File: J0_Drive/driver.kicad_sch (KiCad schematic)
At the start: 7 parts

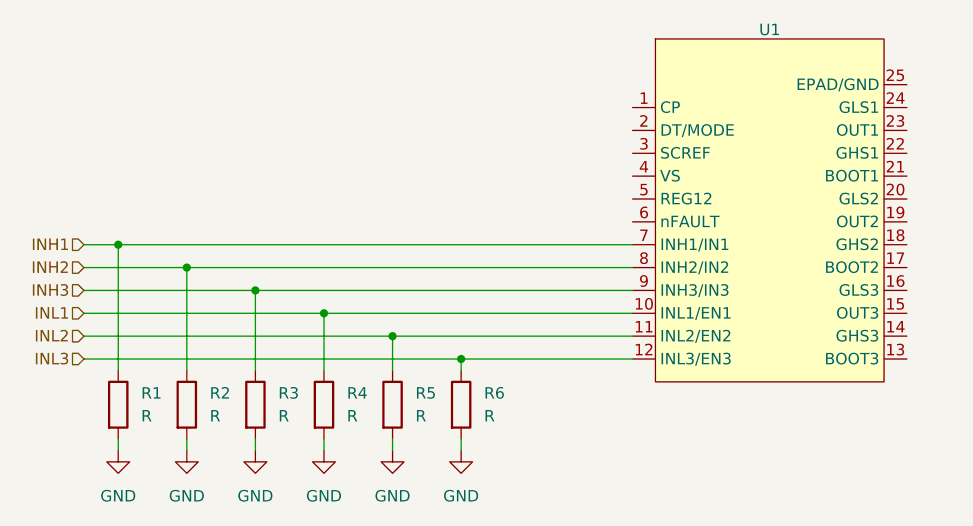
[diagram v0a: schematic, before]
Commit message: added DT/MODE select circuit
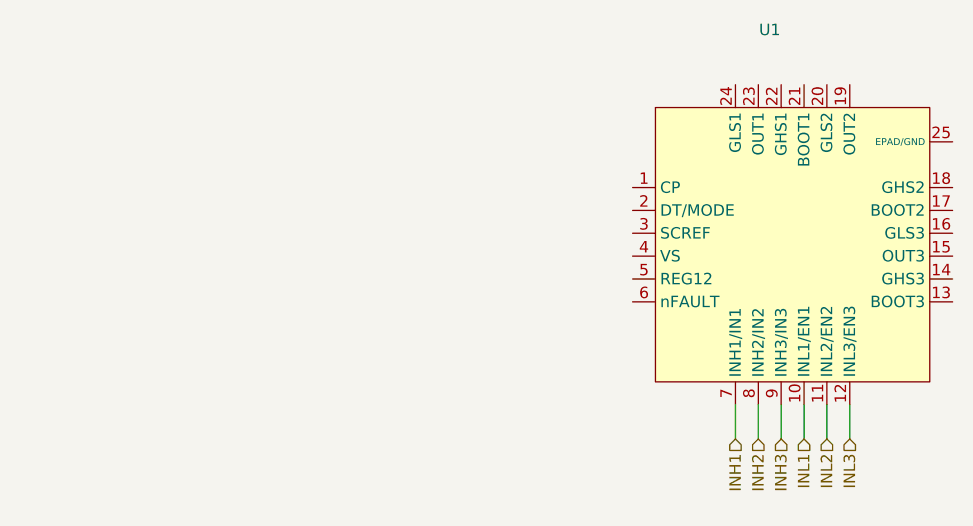
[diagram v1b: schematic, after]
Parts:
- removed R1, R2, R3, R4, R5, R6: R, symbol Device:R
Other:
- moved on the sheet: U1

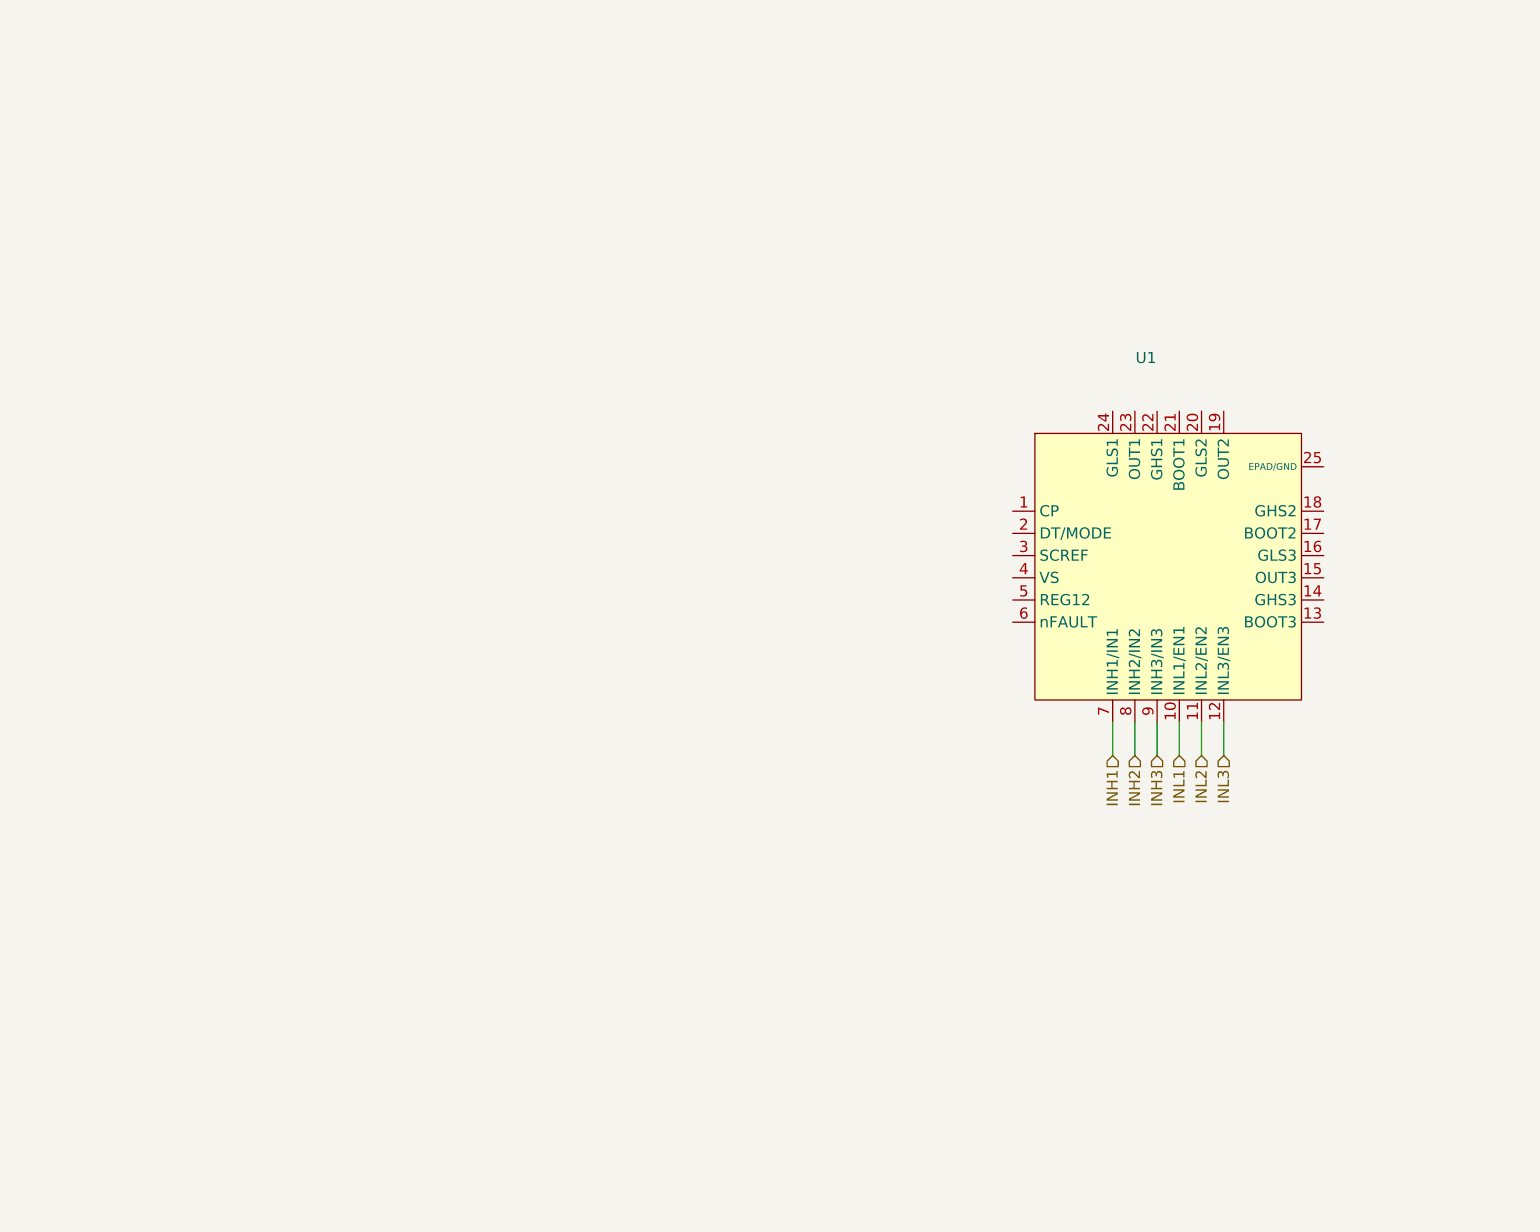
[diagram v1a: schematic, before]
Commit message: added VM supply, REG12, and nFAULT circuit
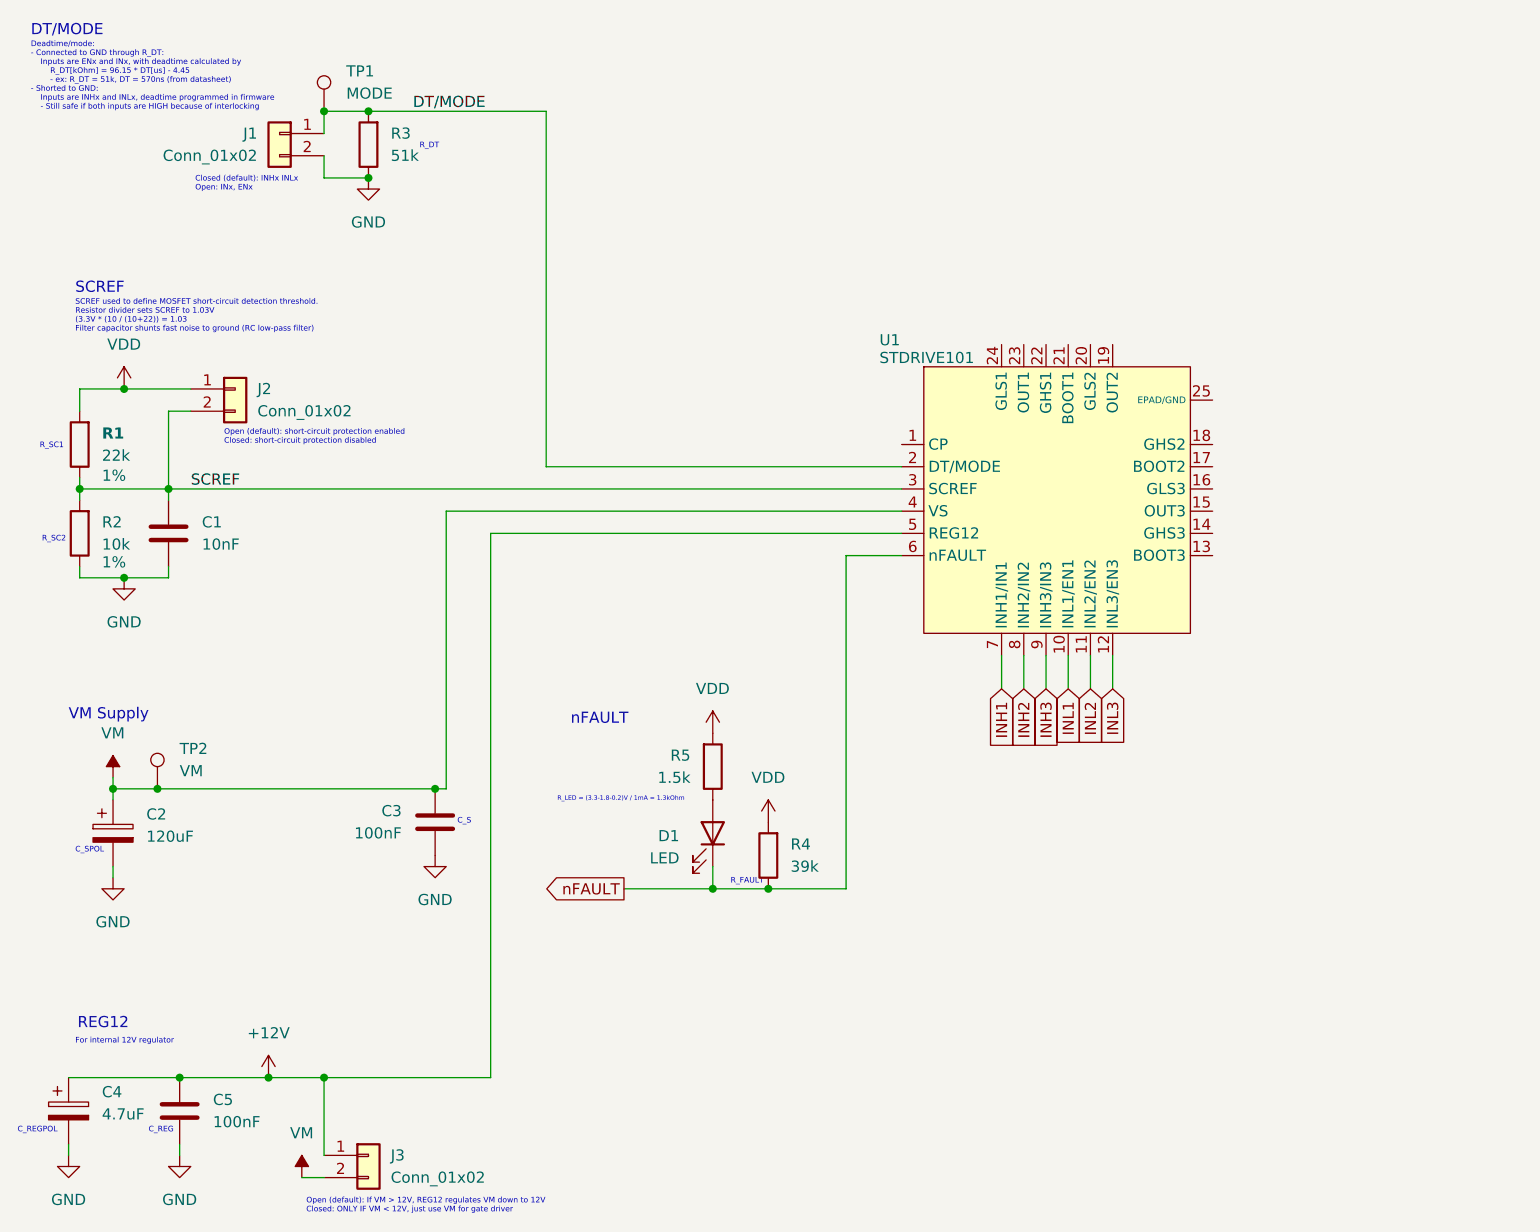
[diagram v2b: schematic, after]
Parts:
- added C1: 10nF, symbol Device:C
- added C2: 120uF, symbol Device:C_Polarized
- added C3, C5: 100nF, symbol Device:C
- added C4: 4.7uF, symbol Device:C_Polarized
- added D1: LED, symbol Device:LED
- added J1, J2, J3: Conn_01x02, symbol Connector_Generic:Conn_01x02
- added R1: 22k, symbol Device:R
- added R2: 10k, symbol Device:R
- added R3: 51k, symbol Device:R
- added R4: 39k, symbol Device:R
- added R5: 1.5k, symbol Device:R
- added TP1: MODE, symbol Connector:TestPoint
- added TP2: VM, symbol Connector:TestPoint
- U1: value (none) -> STDRIVE101
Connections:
- net DT/MODE: now reaches U1.2 (DT/MODE)
- net DT/MODE: now also J1.1 (Pin_1), R3.2, TP1.1
- net SCREF: now reaches U1.3 (SCREF)
- net SCREF: now also C1.1, J2.2 (Pin_2), R1.1, R2.2
- net VM: now reaches U1.4 (VS)
- net VM: now also C2.1, C3.1, J3.2 (Pin_2), TP2.1
- net +12V: now reaches U1.5 (REG12)
- net +12V: now also C4.1, C5.1, J3.1 (Pin_1)
- net nFAULT: now reaches U1.6 (nFAULT)
- net nFAULT: now also D1.1 (K), R4.1
- new net: D1.2 (A), R5.1
- new net GND: C1.2, C2.2, C3.2, C4.2, C5.2, J1.2 (Pin_2), R2.1, R3.1
- new net VDD: J2.1 (Pin_1), R1.2, R4.2, R5.2
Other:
- note added: "C_REG"
- note added: "C_REGPOL"
- note added: "C_S"
- note added: "C_SPOL"
- note added: "Closed (default): INHx INLx Open: INx, ENx"
- note added: "DT/MODE"
- note added: "Deadtime/mode: - Connected to GND through R_DT: Inputs are ENx and INx, with deadtime calculated by R_DT[kOhm] = 96.15 * DT[us] - 4.45 - ex: R_DT = 51k, DT = 570ns (from datasheet) - Shorted to GND: Inputs are INHx and INLx, deadtime programmed in firmware - Still safe if both inputs are HIGH because of interlocking"
- note added: "For internal 12V regulator"
- note added: "Open (default): If VM > 12V, REG12 regulates VM down to 12V Closed: ONLY IF VM < 12V, just use VM for gate driver"
- note added: "Open (default): short-circuit protection enabled Closed: short-circuit protection disabled"
- note added: "REG12"
- note added: "R_DT"
- note added: "R_FAULT"
- note added: "R_LED = (3.3-1.8-0.2)V / 1mA = 1.3kOhm"
- note added: "R_SC1"
- note added: "R_SC2"
- note added: "SCREF"
- note added: "SCREF used to define MOSFET short-circuit detection threshold. Resistor divider sets SCREF to 1.03V (3.3V * (10 / (10+22)) = 1.03 Filter capacitor shunts fast noise to ground (RC low-pass filter)"
- note added: "VM Supply"
- note added: "nFAULT"

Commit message: finished first design of driver page
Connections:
- net GND: now also U1.25 (EPAD/GND)
- net CP: now reaches U1.1 (CP)
- net BOOT3: now reaches U1.13 (BOOT3)
- net GHS3: now reaches U1.14 (GHS3)
- net OUT3: now reaches U1.15 (OUT3)
- net GLS3: now reaches U1.16 (GLS3)
- net BOOT2: now reaches U1.17 (BOOT2)
- net GHS2: now reaches U1.18 (GHS2)
- net OUT2: now reaches U1.19 (OUT2)
- net GLS2: now reaches U1.20 (GLS2)
- net BOOT1: now reaches U1.21 (BOOT1)
- net GHS1: now reaches U1.22 (GHS1)
- net OUT1: now reaches U1.23 (OUT1)
- net GLS1: now reaches U1.24 (GLS1)
- net INH1 renamed INH1/IN1
- net INH2 renamed INH2/IN2
- net INH3 renamed INH3/IN3
- net INL1 renamed INL1/EN1
- net INL2 renamed INL2/EN2
- net INL3 renamed INL3/EN3
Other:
- moved on the sheet: C1, C2, C3, C4, C5, D1, J1, J2, J3, R1, R2, R3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

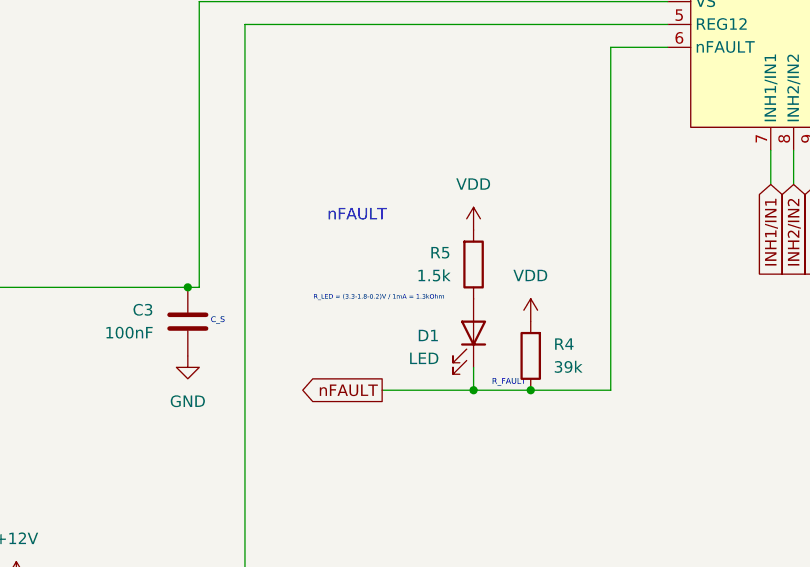
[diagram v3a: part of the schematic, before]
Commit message: finished first design of power stage page
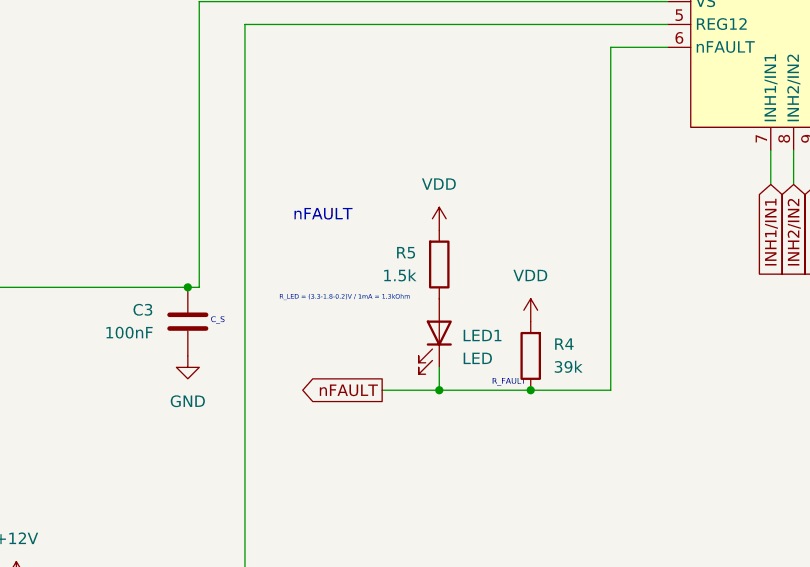
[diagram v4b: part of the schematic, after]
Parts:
- renumbered D1 to LED1
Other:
- moved on the sheet: LED1, R5
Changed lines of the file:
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@@
 	(text "nFAULT"
 		(exclude_from_sim no)
-		(at 112.014 115.824 0)
+		(at 108.204 115.824 0)
 		(effects
 			(font
@@
 	(text "R_LED = (3.3-1.8-0.2)V / 1mA = 1.3kOhm"
 		(exclude_from_sim no)
-		(at 110.49 125.73 0)
+		(at 106.68 125.73 0)
 		(effects
 			(font
@@
 	)
 	(junction
-		(at 88.9 46.99)
+		(at 124.46 135.89)
 		(diameter 0)
 		(color 0 0 0 0)
 	)
 	(junction
-		(at 60.96 78.74)
+		(at 88.9 46.99)
 		(diameter 0)
 		(color 0 0 0 0)
 	)
 	(junction
-		(at 96.52 124.46)
+		(at 60.96 78.74)
 		(diameter 0)
 		(color 0 0 0 0)
 	)
 	(junction
-		(at 128.27 135.89)
+		(at 96.52 124.46)
 		(diameter 0)
 		(color 0 0 0 0)
@@
 	(wire
 		(pts
-			(xy 128.27 133.35) (xy 128.27 135.89)
+			(xy 124.46 133.35) (xy 124.46 135.89)
 		)
 		(stroke
@@
 	(wire
 		(pts
+			(xy 124.46 135.89) (xy 134.62 135.89)
+		)
+		(stroke
+			(width 0)
+			(type default)
+		)
+	)
+	(wire
+		(pts
 			(xy 66.04 90.17) (xy 66.04 91.44)
 		)
@@
 	(wire
 		(pts
-			(xy 128.27 135.89) (xy 134.62 135.89)
-		)
-		(stroke
-			(width 0)
-			(type default)
-		)
-	)
-	(wire
-		(pts
 			(xy 66.04 90.17) (xy 149.86 90.17)
 		)
@@
 	(wire
 		(pts
-			(xy 118.11 135.89) (xy 128.27 135.89)
+			(xy 118.11 135.89) (xy 124.46 135.89)
 		)
 		(stroke
@@
 	(symbol
 		(lib_id "Device:R")
-		(at 128.27 121.92 0)
+		(at 124.46 121.92 0)
 		(mirror x)
 		(unit 1)
@@
 		(fields_autoplaced yes)
 		(property "Reference" "R5"
-			(at 125.73 120.6499 0)
+			(at 121.92 120.6499 0)
 			(show_name no)
 			(do_not_autoplace no)
@@
 		)
 		(property "Value" "1.5k"
-			(at 125.73 123.1899 0)
+			(at 121.92 123.1899 0)
 			(show_name no)
 			(do_not_autoplace no)
@@
 		)
 		(property "Footprint" ""
-			(at 126.492 121.92 90)
+			(at 122.682 121.92 90)
 			(hide yes)
 			(show_name no)
@@
 		)
 		(property "Datasheet" ""
-			(at 128.27 121.92 0)
+			(at 124.46 121.92 0)
 			(hide yes)
 			(show_name no)
@@
 		)
 		(property "Description" "Resistor"
-			(at 128.27 121.92 0)
+			(at 124.46 121.92 0)
 			(hide yes)
 			(show_name no)
@@
 	(symbol
 		(lib_id "Device:LED")
-		(at 128.27 129.54 270)
+		(at 124.46 129.54 270)
 		(mirror x)
 		(unit 1)
@@
 		(dnp no)
 		(fields_autoplaced yes)
-		(property "Reference" "D1"
-			(at 124.46 129.8574 90)
+		(property "Reference" "LED1"
+			(at 127 129.8574 90)
 			(show_name no)
 			(do_not_autoplace no)
@@
 					(size 1.27 1.27)
 				)
-				(justify right)
+				(justify left)
 			)
 		)
 		(property "Value" "LED"
-			(at 124.46 132.3974 90)
+			(at 127 132.3974 90)
 			(show_name no)
 			(do_not_autoplace no)
@@
 					(size 1.27 1.27)
 				)
-				(justify right)
+				(justify left)
 			)
 		)
 		(property "Footprint" ""
-			(at 128.27 129.54 0)
+			(at 124.46 129.54 0)
 			(hide yes)
 			(show_name no)
@@
 		)
 		(property "Datasheet" ""
-			(at 128.27 129.54 0)
+			(at 124.46 129.54 0)
 			(hide yes)
 			(show_name no)
@@
 		)
 		(property "Description" "Light emitting diode"
-			(at 128.27 129.54 0)
+			(at 124.46 129.54 0)
 			(hide yes)
 			(show_name no)
@@
 		)
 		(property "Sim.Pins" "1=K 2=A"
-			(at 128.27 129.54 0)
+			(at 124.46 129.54 0)
 			(hide yes)
 			(show_name no)
@@
 			(project "J0_Drive"
 				(path "/00bb46ee-9cfb-4ad9-9820-c6d5e19a8f16/35f45dbe-0272-466f-a35a-2618a5161648"
-					(reference "D1")
+					(reference "LED1")
 					(unit 1)
 				)
@@
 	(symbol
 		(lib_id "power:VDD")
-		(at 128.27 118.11 0)
+		(at 124.46 118.11 0)
 		(mirror y)
 		(unit 1)
@@
 		(fields_autoplaced yes)
 		(property "Reference" "#PWR012"
-			(at 128.27 121.92 0)
+			(at 124.46 121.92 0)
 			(hide yes)
 			(show_name no)
@@
 		)
 		(property "Value" "VDD"
-			(at 128.27 113.03 0)
+			(at 124.46 113.03 0)
 			(show_name no)
 			(do_not_autoplace no)
@@
 		)
 		(property "Footprint" ""
-			(at 128.27 118.11 0)
+			(at 124.46 118.11 0)
 			(hide yes)
 			(show_name no)
@@
 		)
 		(property "Datasheet" ""
-			(at 128.27 118.11 0)
+			(at 124.46 118.11 0)
 			(hide yes)
 			(show_name no)
@@
 		)
 		(property "Description" "Power symbol creates a global label with name \"VDD\""
-			(at 128.27 118.11 0)
+			(at 124.46 118.11 0)
 			(hide yes)
 			(show_name no)

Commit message: finished half bridges, started mcu
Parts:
- C2, C3: Voltage Rating (none) -> 100V
- C4, C5: Voltage Rating (none) -> 25V
- R1: value 22k -> 18k
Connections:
- net CP is gone; now on net GND: U1.1 (CP)
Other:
- note added: "CP Overcurrent protection designed for use with low-side sensing, so this just disables it (will use comparator in mcu with the inline current sense outputs)"
- note added: "SCREF used to define MOSFET short-circuit detection threshold. Resistor divider sets SCREF: (3.3V * (10 / (10+18)) = 1.18 V Filter capacitor shunts fast noise to ground (RC low-pass filter)"
- note removed: "SCREF used to define MOSFET short-circuit detection threshold. Resistor divider sets SCREF to 1.03V (3.3V * (10 / (10+22)) = 1.03 Filter capacitor shunts fast noise to ground (RC low-pass filter)"
